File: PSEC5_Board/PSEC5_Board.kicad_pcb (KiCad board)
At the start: 2 copper layers, 76.2 x 76.2 mm, 187 parts, among them IC1 LTC6409IUDB#TRMPBF, IC2 LTC6409IUDB#TRMPBF, IC3 LTC6409IUDB#TRMPBF, IC4 LTC6409IUDB#TRMPBF, IC5 LTC6409IUDB#TRMPBF, IC6 LTC6409IUDB#TRMPBF, IC7 LTC6409IUDB#TRMPBF, IC8 LTC6409IUDB#TRMPBF, J1 QTH-040-01-X-D-DP-A, J11 Conn_Coaxial, J2 Conn_Coaxial, J3 Conn_Coaxial, J4 Conn_Coaxial, J5 Conn_Coaxial, J6 Conn_Coaxial, J7 Conn_Coaxial, J8 Conn_Coaxial, J9 QTH-040-01-X-D-DP-A, U1 MCP1700T-1802E_TT, U3 DAC8411IDCKT, U5 MC100LVEL, U6 OPA607QDBVRQ1, U7 AD4008BCPZ-RL7, Y1 ASE2-40.000MHZ-ET

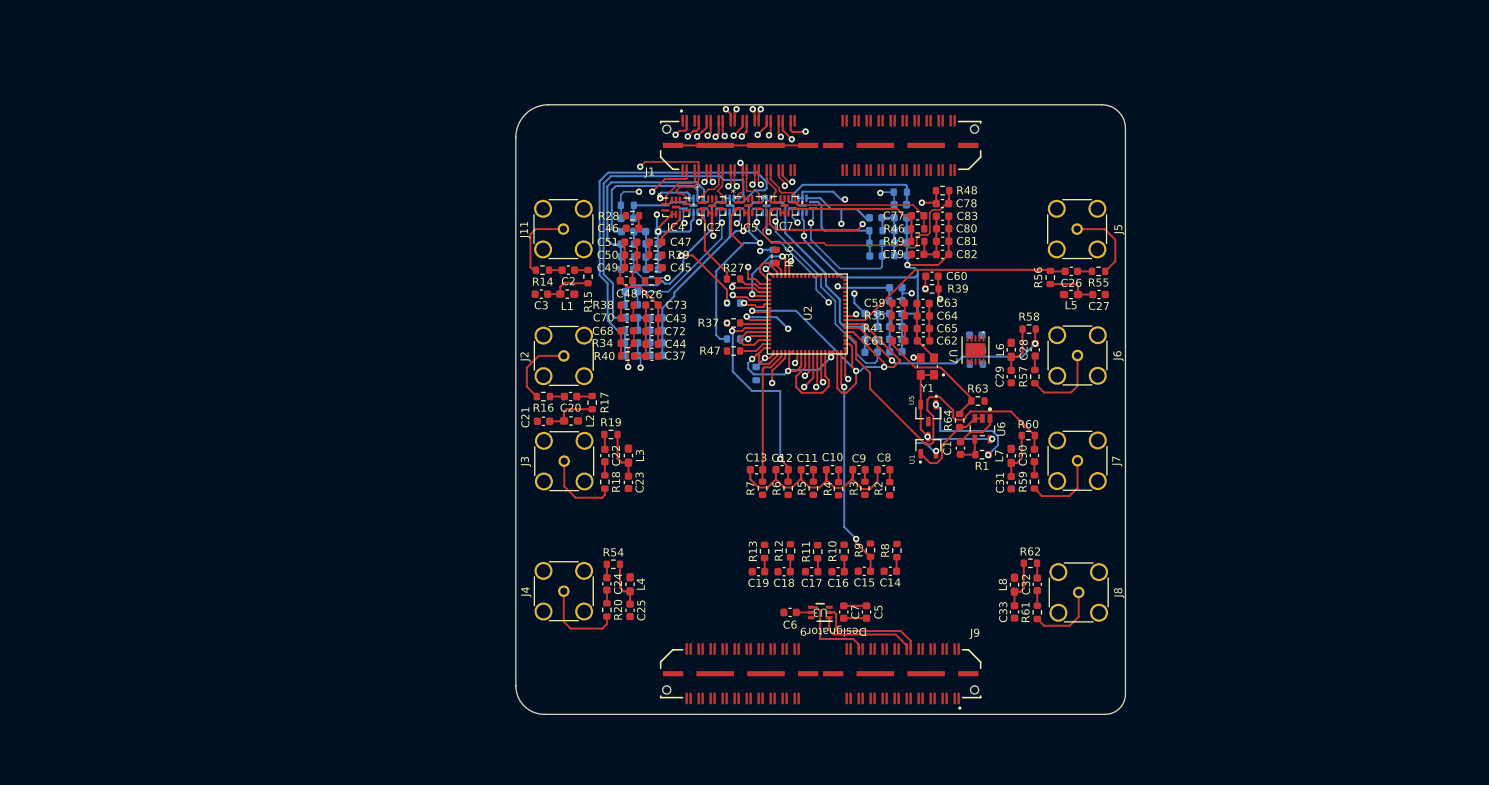
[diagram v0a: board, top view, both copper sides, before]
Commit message: DUT Layout Overhaul
Footprints need to be replaced.
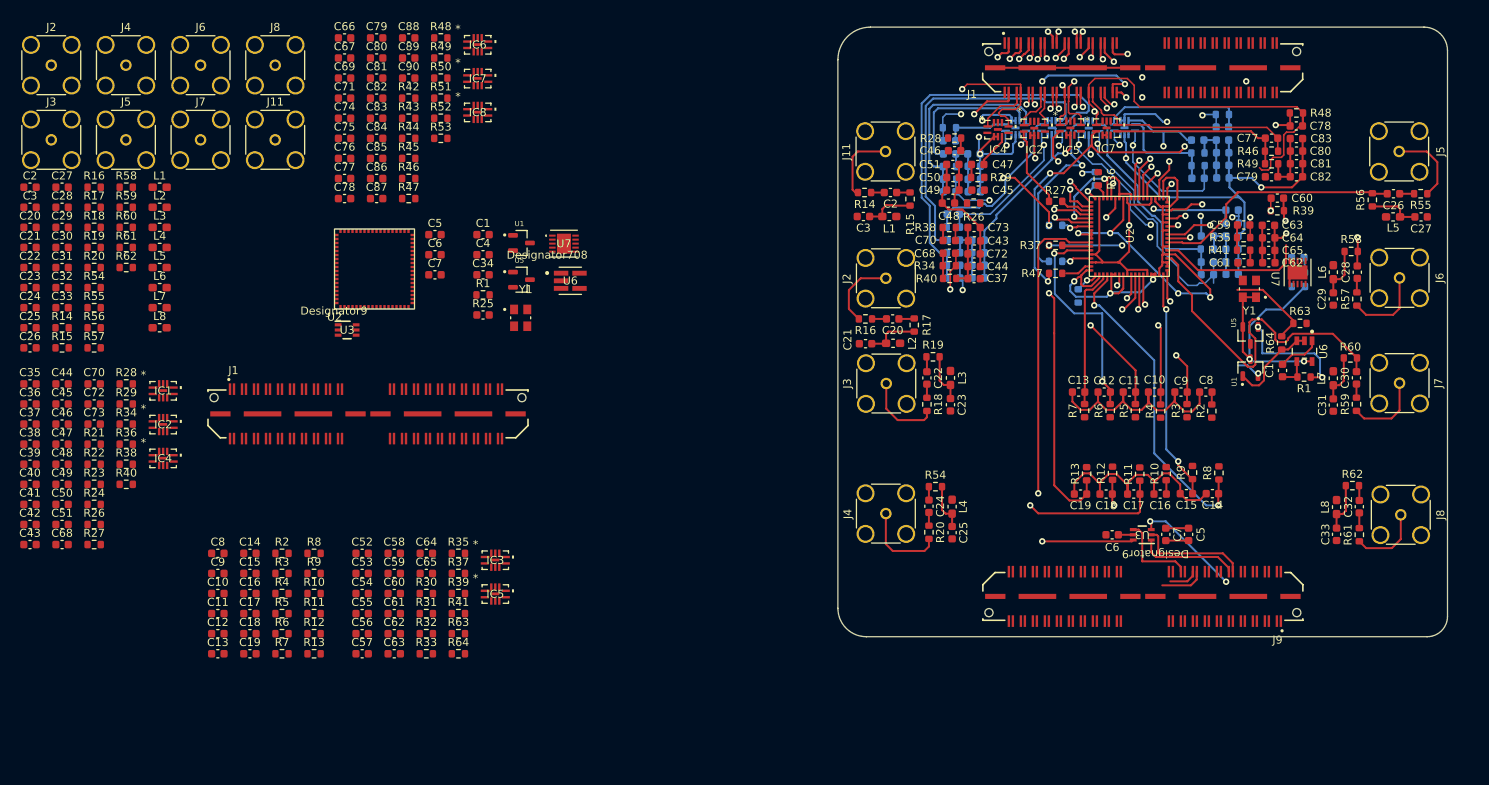
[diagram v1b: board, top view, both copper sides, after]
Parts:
- removed the C1 at (168.1, 81.5)
- removed the C10 at (152.1, 84.2)
- removed the C11 at (149.0, 84.2)
- removed the C12 at (145.8, 84.2)
- removed the C13 at (142.6, 84.2)
- removed the C14 at (159.4, 96.9)
- removed the C15 at (156.1, 96.9)
- removed the C16 at (152.8, 96.9)
- removed the C17 at (149.5, 96.9)
- removed the C18 at (146.1, 96.9)
- removed the C19 at (142.9, 96.9)
- removed the C2 at (119.1, 59.2)
- removed the C20 at (119.4, 75.0)
- removed the C21 at (116.0, 78.1)
- removed the C22 at (123.7, 82.4)
- removed the C23 at (126.6, 85.8)
- removed the C24 at (123.9, 98.4)
- removed the C25 at (126.8, 101.7)
- removed the C26 at (182.0, 59.4)
- removed the C27 at (185.4, 62.3)
- removed the C28 at (177.5, 69.2)
- removed the C29 at (174.5, 72.5)
- removed the C3 at (115.7, 62.2)
- removed the C30 at (177.4, 82.4)
- removed the C31 at (174.5, 85.8)
- removed the C32 at (177.7, 98.5)
- removed the C33 at (174.9, 101.9)
- removed the C34 at (170.0, 67.4)
- removed the C35 at (126.5, 59.1)
- removed the C36 at (126.5, 52.7)
- removed the C37 at (129.6, 70.0)
- removed the C38 at (126.5, 54.4)
- removed the C39 at (129.6, 55.9)
- removed the C4 at (170.1, 69.2)
- removed the C40 at (129.6, 57.6)
- removed the C41 at (129.6, 59.1)
- removed the C42 at (129.5, 54.4)
- removed the C43 at (129.6, 65.3)
- removed the C44 at (129.6, 68.5)
- removed the C45 at (130.1, 58.9)
- removed the C46 at (127.1, 54.0)
- removed the C47 at (130.0, 55.7)
- removed the C48 at (126.4, 60.5)
- removed the C49 at (126.9, 58.9)
- removed the C5 at (156.4, 102.0)
- removed the C50 at (126.9, 57.3)
- removed the C51 at (126.9, 55.7)
- removed the C52 at (127.0, 69.9)
- removed the C53 at (127.0, 61.9)
- removed the C54 at (127.0, 65.2)
- removed the C55 at (130.1, 65.2)
- removed the C56 at (130.1, 66.8)
- removed the C57 at (130.1, 68.3)
- removed the C58 at (130.1, 69.9)
- removed the C59 at (160.3, 63.3)
- removed the C6 at (146.8, 102.0)
- removed the C60 at (164.6, 60.0)
- removed the C61 at (160.4, 68.1)
- removed the C62 at (163.5, 68.1)
- removed the C63 at (163.4, 63.4)
- removed the C64 at (163.5, 64.9)
- removed the C65 at (163.5, 66.5)
- removed the C66 at (156.9, 69.5)
- removed the C67 at (160.0, 61.4)
- removed the C68 at (126.5, 66.8)
- removed the C69 at (157.0, 64.7)
- removed the C7 at (153.5, 102.0)
- removed the C70 at (126.5, 65.2)
- removed the C71 at (160.0, 69.4)
- removed the C72 at (129.6, 66.9)
- removed the C73 at (129.6, 63.6)
- removed the C74 at (160.0, 64.7)
- removed the C75 at (160.0, 67.9)
- removed the C76 at (160.0, 66.3)
- removed the C77 at (162.8, 52.4)
- removed the C78 at (165.9, 50.9)
- removed the C79 at (162.8, 57.3)
- removed the C8 at (158.5, 84.2)
- removed the C80 at (165.9, 54.0)
- removed the C81 at (165.9, 55.6)
- removed the C82 at (165.9, 57.3)
- removed the C83 at (165.9, 52.5)
- removed the C84 at (157.6, 57.4)
- removed the C85 at (160.6, 51.0)
- removed the C86 at (157.5, 52.7)
- removed the C87 at (160.6, 55.8)
- removed the C88 at (160.6, 54.2)
- removed the C89 at (160.6, 52.7)
- removed the C9 at (155.4, 84.2)
- removed the C90 at (160.7, 57.4)
- removed the IC1 at (134.8, 51.1)
- removed the IC2 at (137.1, 51.2)
- removed the IC3 at (139.3, 51.1)
- removed the IC4 at (132.5, 51.4)
- removed the IC5 at (141.6, 51.2)
- removed the IC6 at (143.9, 51.1)
- removed the IC7 at (146.1, 51.2)
- removed the IC8 at (148.4, 51.1)
- removed the J1 at (150.6, 43.6)
- removed the J11 at (118.5, 54.1)
- removed the J2 at (118.5, 69.9)
- removed the J3 at (118.6, 83.1)
- removed the J4 at (118.5, 99.4)
- removed the J5 at (182.7, 54.1)
- removed the J6 at (182.7, 69.9)
- removed the J7 at (182.7, 83.0)
- removed the J8 at (182.9, 99.5)
- removed the L1 at (119.0, 62.2)
- removed the L2 at (119.4, 78.1)
- removed the L3 at (126.6, 82.4)
- removed the L4 at (126.8, 98.5)
- removed the L5 at (181.9, 62.3)
- removed the L6 at (174.5, 69.2)
- removed the L7 at (174.5, 82.4)
- removed the L8 at (174.9, 98.5)
- removed the R1 at (170.8, 82.3)
- removed the R10 at (153.6, 94.4)
- removed the R11 at (150.3, 94.4)
- removed the R12 at (146.9, 94.3)
- removed the R13 at (143.6, 94.4)
- removed the R14 at (115.9, 59.2)
- removed the R15 at (121.6, 60.0)
- removed the R16 at (116.0, 75.0)
- removed the R17 at (122.1, 75.8)
- removed the R18 at (123.7, 85.7)
- removed the R19 at (124.4, 79.8)
- removed the R2 at (159.3, 86.5)
- removed the R20 at (123.9, 101.7)
- removed the R21 at (126.5, 57.5)
- removed the R22 at (144.7, 57.5)
- removed the R23 at (126.5, 51.1)
- removed the R24 at (126.5, 56.0)
- removed the R25 at (170.1, 71.0)
- removed the R26 at (129.5, 60.5)
- removed the R27 at (139.8, 60.3)
- removed the R28 at (127.1, 52.4)
- removed the R29 at (130.0, 57.3)
- removed the R3 at (156.2, 86.5)
- removed the R30 at (127.0, 68.3)
- removed the R31 at (139.8, 63.3)
- removed the R32 at (127.0, 63.5)
- removed the R33 at (127.0, 66.7)
- removed the R34 at (126.5, 68.4)
- removed the R35 at (160.3, 64.9)
- removed the R36 at (145.1, 57.5)
- removed the R37 at (139.8, 65.8)
- removed the R38 at (126.5, 63.6)
- removed the R39 at (164.6, 61.6)
- removed the R4 at (152.9, 86.5)
- removed the R40 at (126.5, 70.0)
- removed the R41 at (160.3, 66.5)
- removed the R42 at (156.9, 67.9)
- removed the R43 at (139.8, 67.8)
- removed the R44 at (160.0, 63.0)
- removed the R45 at (156.9, 66.3)
- removed the R46 at (162.8, 54.1)
- removed the R47 at (139.8, 69.3)
- removed the R48 at (165.9, 49.3)
- removed the R49 at (162.8, 55.6)
- removed the R5 at (149.7, 86.5)
- removed the R50 at (157.6, 55.9)
- removed the R51 at (142.6, 72.1)
- removed the R52 at (160.6, 49.5)
- removed the R53 at (157.5, 54.3)
- removed the R54 at (124.7, 96.0)
- removed the R55 at (185.4, 59.4)
- removed the R56 at (179.3, 60.1)
- removed the R57 at (177.4, 72.5)
- removed the R58 at (176.7, 66.6)
- removed the R59 at (177.4, 85.7)
- removed the R6 at (146.6, 86.5)
- removed the R60 at (176.6, 79.9)
- removed the R61 at (177.7, 102.0)
- removed the R62 at (176.9, 95.9)
- removed the R63 at (170.3, 75.6)
- removed the R64 at (168.0, 78.0)
- removed the R7 at (143.4, 86.5)
- removed the R8 at (160.2, 94.3)
- removed the R9 at (156.9, 94.2)
- removed the U1 at (164.1, 81.1)
- removed the U2 at (154.0, 59.7)
- removed the U3 at (150.6, 102.0)
- removed the U5 at (164.1, 77.1)
- removed the U6 at (170.9, 79.1)
- removed the U7 at (170.0, 69.2)
- removed the Y1 at (164.0, 71.3)
- added C1: C, Capacitor_SMD:C_0603_1608Metric, F.Cu at (108.4, 54.8)
- added C1: C, Capacitor_SMD:C_0603_1608Metric, F.Cu at (208.4, 71.8)
- added C10: C, Capacitor_SMD:C_0603_1608Metric, F.Cu at (192.4, 74.5)
- added C10: C, Capacitor_SMD:C_0603_1608Metric, F.Cu at (75.3, 99.6)
- added C11: C, Capacitor_SMD:C_0603_1608Metric, F.Cu at (75.3, 102.2)
- added C11: C, Capacitor_SMD:C_0603_1608Metric, F.Cu at (189.2, 74.5)
- added C12: C, Capacitor_SMD:C_0603_1608Metric, F.Cu at (75.3, 104.7)
- added C12: C, Capacitor_SMD:C_0603_1608Metric, F.Cu at (186.1, 74.5)
- added C13: C, Capacitor_SMD:C_0603_1608Metric, F.Cu at (75.3, 107.2)
- added C13: C, Capacitor_SMD:C_0603_1608Metric, F.Cu at (182.9, 74.5)
- added C14: C, Capacitor_SMD:C_0603_1608Metric, F.Cu at (79.3, 94.6)
- added C14: C, Capacitor_SMD:C_0603_1608Metric, F.Cu at (199.6, 87.2)
- added C15: C, Capacitor_SMD:C_0603_1608Metric, F.Cu at (79.3, 97.1)
- added C15: C, Capacitor_SMD:C_0603_1608Metric, F.Cu at (196.4, 87.2)
- added C16: C, Capacitor_SMD:C_0603_1608Metric, F.Cu at (193.1, 87.2)
- added C16: C, Capacitor_SMD:C_0603_1608Metric, F.Cu at (79.3, 99.6)
- added C17: C, Capacitor_SMD:C_0603_1608Metric, F.Cu at (79.3, 102.2)
- added C17: C, Capacitor_SMD:C_0603_1608Metric, F.Cu at (189.8, 87.2)
- added C18: C, Capacitor_SMD:C_0603_1608Metric, F.Cu at (186.3, 87.2)
- added C18: C, Capacitor_SMD:C_0603_1608Metric, F.Cu at (79.3, 104.7)
- added C19: C, Capacitor_SMD:C_0603_1608Metric, F.Cu at (183.1, 87.2)
- added C19: C, Capacitor_SMD:C_0603_1608Metric, F.Cu at (79.3, 107.2)
- added C2: 100n, Capacitor_SMD:C_0603_1608Metric, F.Cu at (51.8, 48.9)
- added C2: 100n, Capacitor_SMD:C_0603_1608Metric, F.Cu at (159.4, 49.5)
- added C20: 100n, Capacitor_SMD:C_0603_1608Metric, F.Cu at (51.8, 53.9)
- added C20: 100n, Capacitor_SMD:C_0603_1608Metric, F.Cu at (159.6, 65.3)
- added C21: 100n, Capacitor_SMD:C_0603_1608Metric, F.Cu at (51.8, 56.4)
- added C21: 100n, Capacitor_SMD:C_0603_1608Metric, F.Cu at (156.3, 68.4)
- added C22: 100n, Capacitor_SMD:C_0603_1608Metric, F.Cu at (163.9, 72.7)
- added C22: 100n, Capacitor_SMD:C_0603_1608Metric, F.Cu at (51.8, 58.9)
- added C23: 100n, Capacitor_SMD:C_0603_1608Metric, F.Cu at (51.8, 61.4)
- added C23: 100n, Capacitor_SMD:C_0603_1608Metric, F.Cu at (166.9, 76.0)
- added C24: 100n, Capacitor_SMD:C_0603_1608Metric, F.Cu at (164.2, 88.7)
- added C24: 100n, Capacitor_SMD:C_0603_1608Metric, F.Cu at (51.8, 63.9)
- added C25: 100n, Capacitor_SMD:C_0603_1608Metric, F.Cu at (51.8, 66.4)
- added C25: 100n, Capacitor_SMD:C_0603_1608Metric, F.Cu at (167.1, 92.0)
- added C26: 100n, Capacitor_SMD:C_0603_1608Metric, F.Cu at (51.8, 68.9)
- added C26: 100n, Capacitor_SMD:C_0603_1608Metric, F.Cu at (222.2, 49.7)
- added C27: 100n, Capacitor_SMD:C_0603_1608Metric, F.Cu at (55.8, 48.9)
- added C27: 100n, Capacitor_SMD:C_0603_1608Metric, F.Cu at (225.7, 52.6)
- added C28: 100n, Capacitor_SMD:C_0603_1608Metric, F.Cu at (217.7, 59.5)
- added C28: 100n, Capacitor_SMD:C_0603_1608Metric, F.Cu at (55.8, 51.4)
- added C29: 100n, Capacitor_SMD:C_0603_1608Metric, F.Cu at (55.8, 53.9)
- added C29: 100n, Capacitor_SMD:C_0603_1608Metric, F.Cu at (214.7, 62.8)
- added C3: 100n, Capacitor_SMD:C_0603_1608Metric, F.Cu at (51.8, 51.4)
- added C3: 100n, Capacitor_SMD:C_0603_1608Metric, F.Cu at (156.0, 52.5)
- added C30: 100n, Capacitor_SMD:C_0603_1608Metric, F.Cu at (55.8, 56.4)
- added C30: 100n, Capacitor_SMD:C_0603_1608Metric, F.Cu at (217.6, 72.7)
- added C31: 100n, Capacitor_SMD:C_0603_1608Metric, F.Cu at (214.7, 76.1)
- added C31: 100n, Capacitor_SMD:C_0603_1608Metric, F.Cu at (55.8, 58.9)
- added C32: 100n, Capacitor_SMD:C_0603_1608Metric, F.Cu at (55.8, 61.4)
- added C32: 100n, Capacitor_SMD:C_0603_1608Metric, F.Cu at (218.0, 88.8)
- added C33: 100n, Capacitor_SMD:C_0603_1608Metric, F.Cu at (215.1, 92.2)
- added C33: 100n, Capacitor_SMD:C_0603_1608Metric, F.Cu at (55.8, 63.9)
- added C34: C, Capacitor_SMD:C_0603_1608Metric, F.Cu at (108.4, 59.8)
- added C34: C, Capacitor_SMD:C_0603_1608Metric, B.Cu at (210.3, 57.7)
- added C35: 1.3pF, Capacitor_SMD:C_0603_1608Metric, F.Cu at (51.8, 73.4)
- added C35: 1.3pF, Capacitor_SMD:C_0603_1608Metric, B.Cu at (166.8, 49.4)
- added C36: 1.3pF, Capacitor_SMD:C_0603_1608Metric, F.Cu at (51.8, 76.0)
- added C36: 1.3pF, Capacitor_SMD:C_0603_1608Metric, B.Cu at (166.7, 43.0)
- added C37: 0.1u, Capacitor_SMD:C_0603_1608Metric, F.Cu at (169.8, 60.3)
- added C37: 0.1u, Capacitor_SMD:C_0603_1608Metric, F.Cu at (51.8, 78.5)
- added C38: 0.1u, Capacitor_SMD:C_0603_1608Metric, F.Cu at (51.8, 81.0)
- added C38: 0.1u, Capacitor_SMD:C_0603_1608Metric, B.Cu at (166.8, 44.7)
- added C39: 1000pF, Capacitor_SMD:C_0603_1608Metric, F.Cu at (51.8, 83.5)
- added C39: 1000pF, Capacitor_SMD:C_0603_1608Metric, B.Cu at (169.8, 46.2)
- added C4: 0.1 uf, Capacitor_SMD:C_0603_1608Metric, F.Cu at (108.4, 57.3)
- added C4: 0.1 uf, Capacitor_SMD:C_0603_1608Metric, B.Cu at (210.4, 59.5)
- added C40: 0.1uF, Capacitor_SMD:C_0603_1608Metric, F.Cu at (51.8, 86.0)
- added C40: 0.1uF, Capacitor_SMD:C_0603_1608Metric, B.Cu at (169.8, 47.9)
- added C41: 0.1uF, Capacitor_SMD:C_0603_1608Metric, F.Cu at (51.8, 88.5)
- added C41: 0.1uF, Capacitor_SMD:C_0603_1608Metric, B.Cu at (169.9, 49.4)
- added C42: 1000pF, Capacitor_SMD:C_0603_1608Metric, F.Cu at (51.8, 91.0)
- added C42: 1000pF, Capacitor_SMD:C_0603_1608Metric, B.Cu at (169.8, 44.7)
- added C43: 0.1uF, Capacitor_SMD:C_0603_1608Metric, F.Cu at (169.9, 55.6)
- added C43: 0.1uF, Capacitor_SMD:C_0603_1608Metric, F.Cu at (51.8, 93.5)
- added C44: 1000pF, Capacitor_SMD:C_0603_1608Metric, F.Cu at (169.8, 58.8)
- added C44: 1000pF, Capacitor_SMD:C_0603_1608Metric, F.Cu at (55.8, 73.4)
- added C45: 1.3pF, Capacitor_SMD:C_0603_1608Metric, F.Cu at (55.8, 76.0)
- added C45: 1.3pF, Capacitor_SMD:C_0603_1608Metric, F.Cu at (170.3, 49.2)
- added C46: 1.3pF, Capacitor_SMD:C_0603_1608Metric, F.Cu at (167.4, 44.3)
- added C46: 1.3pF, Capacitor_SMD:C_0603_1608Metric, F.Cu at (55.8, 78.5)
- added C47: 0.1u, Capacitor_SMD:C_0603_1608Metric, F.Cu at (170.3, 46.0)
- added C47: 0.1u, Capacitor_SMD:C_0603_1608Metric, F.Cu at (55.8, 81.0)
- added C48: 1000pF, Capacitor_SMD:C_0603_1608Metric, F.Cu at (55.8, 83.5)
- added C48: 1000pF, Capacitor_SMD:C_0603_1608Metric, F.Cu at (166.6, 50.8)
- added C49: 0.1uF, Capacitor_SMD:C_0603_1608Metric, F.Cu at (167.2, 49.2)
- added C49: 0.1uF, Capacitor_SMD:C_0603_1608Metric, F.Cu at (55.8, 86.0)
- added C5: 700n, Capacitor_SMD:C_0603_1608Metric, F.Cu at (196.6, 92.2)
- added C5: 700n, Capacitor_SMD:C_0603_1608Metric, F.Cu at (102.4, 54.8)
- added C50: 0.1uF, Capacitor_SMD:C_0603_1608Metric, F.Cu at (55.8, 88.5)
- added C50: 0.1uF, Capacitor_SMD:C_0603_1608Metric, F.Cu at (167.2, 47.6)
- added C51: 1000pF, Capacitor_SMD:C_0603_1608Metric, F.Cu at (167.2, 46.0)
- added C51: 1000pF, Capacitor_SMD:C_0603_1608Metric, F.Cu at (55.8, 91.0)
- added C52: 1.3pF, Capacitor_SMD:C_0603_1608Metric, F.Cu at (93.3, 94.6)
- added C52: 1.3pF, Capacitor_SMD:C_0603_1608Metric, B.Cu at (167.3, 60.2)
- added C53: 1.3pF, Capacitor_SMD:C_0603_1608Metric, F.Cu at (93.3, 97.1)
- added C53: 1.3pF, Capacitor_SMD:C_0603_1608Metric, B.Cu at (167.2, 52.2)
- added C54: 0.1u, Capacitor_SMD:C_0603_1608Metric, F.Cu at (93.3, 99.6)
- added C54: 0.1u, Capacitor_SMD:C_0603_1608Metric, B.Cu at (167.3, 55.5)
- added C55: 1000pF, Capacitor_SMD:C_0603_1608Metric, F.Cu at (93.3, 102.2)
- added C55: 1000pF, Capacitor_SMD:C_0603_1608Metric, B.Cu at (170.3, 55.5)
- added C56: 0.1uF, Capacitor_SMD:C_0603_1608Metric, F.Cu at (93.3, 104.7)
- added C56: 0.1uF, Capacitor_SMD:C_0603_1608Metric, B.Cu at (170.3, 57.1)
- added C57: 0.1uF, Capacitor_SMD:C_0603_1608Metric, F.Cu at (93.3, 107.2)
- added C57: 0.1uF, Capacitor_SMD:C_0603_1608Metric, B.Cu at (170.4, 58.6)
- added C58: 1000pF, Capacitor_SMD:C_0603_1608Metric, F.Cu at (97.3, 94.6)
- added C58: 1000pF, Capacitor_SMD:C_0603_1608Metric, B.Cu at (170.4, 60.2)
- added C59: 1.3pF, Capacitor_SMD:C_0603_1608Metric, F.Cu at (203.5, 53.6)
- added C59: 1.3pF, Capacitor_SMD:C_0603_1608Metric, F.Cu at (97.3, 97.1)
- added C6: 400n, Capacitor_SMD:C_0603_1608Metric, F.Cu at (102.4, 57.3)
- added C6: 400n, Capacitor_SMD:C_0603_1608Metric, F.Cu at (187.1, 92.3)
- added C60: 1.3pF, Capacitor_SMD:C_0603_1608Metric, F.Cu at (97.3, 99.6)
- added C60: 1.3pF, Capacitor_SMD:C_0603_1608Metric, F.Cu at (207.7, 50.2)
- added C61: 0.1u, Capacitor_SMD:C_0603_1608Metric, F.Cu at (203.6, 58.3)
- added C61: 0.1u, Capacitor_SMD:C_0603_1608Metric, F.Cu at (97.3, 102.2)
- added C62: 1000pF, Capacitor_SMD:C_0603_1608Metric, F.Cu at (206.7, 58.3)
- added C62: 1000pF, Capacitor_SMD:C_0603_1608Metric, F.Cu at (97.3, 104.7)
- added C63: 0.1uF, Capacitor_SMD:C_0603_1608Metric, F.Cu at (97.3, 107.2)
- added C63: 0.1uF, Capacitor_SMD:C_0603_1608Metric, F.Cu at (206.6, 53.6)
- added C64: 0.1uF, Capacitor_SMD:C_0603_1608Metric, F.Cu at (101.4, 94.6)
- added C64: 0.1uF, Capacitor_SMD:C_0603_1608Metric, F.Cu at (206.6, 55.2)
- added C65: 1000pF, Capacitor_SMD:C_0603_1608Metric, F.Cu at (206.6, 56.8)
- added C65: 1000pF, Capacitor_SMD:C_0603_1608Metric, F.Cu at (101.4, 97.1)
- added C66: 1.3pF, Capacitor_SMD:C_0603_1608Metric, F.Cu at (91.1, 30.2)
- added C66: 1.3pF, Capacitor_SMD:C_0603_1608Metric, B.Cu at (199.0, 59.8)
- added C67: 1.3pF, Capacitor_SMD:C_0603_1608Metric, F.Cu at (91.1, 32.7)
- added C67: 1.3pF, Capacitor_SMD:C_0603_1608Metric, B.Cu at (202.1, 51.7)
- added C68: 1.3pF, Capacitor_SMD:C_0603_1608Metric, F.Cu at (166.7, 57.1)
- added C68: 1.3pF, Capacitor_SMD:C_0603_1608Metric, F.Cu at (55.8, 93.5)
- added C69: 0.1u, Capacitor_SMD:C_0603_1608Metric, F.Cu at (91.1, 35.2)
- added C69: 0.1u, Capacitor_SMD:C_0603_1608Metric, B.Cu at (199.0, 55.0)
- added C7: 100n, Capacitor_SMD:C_0603_1608Metric, F.Cu at (102.4, 59.8)
- added C7: 100n, Capacitor_SMD:C_0603_1608Metric, F.Cu at (193.8, 92.2)
- added C70: 1.3pF, Capacitor_SMD:C_0603_1608Metric, F.Cu at (59.8, 73.4)
- added C70: 1.3pF, Capacitor_SMD:C_0603_1608Metric, F.Cu at (166.7, 55.5)
- added C71: 1000pF, Capacitor_SMD:C_0603_1608Metric, F.Cu at (91.1, 37.7)
- added C71: 1000pF, Capacitor_SMD:C_0603_1608Metric, B.Cu at (202.1, 59.7)
- added C72: 1000pF, Capacitor_SMD:C_0603_1608Metric, F.Cu at (169.8, 57.2)
- added C72: 1000pF, Capacitor_SMD:C_0603_1608Metric, F.Cu at (59.8, 76.0)
- added C73: 0.1uF, Capacitor_SMD:C_0603_1608Metric, F.Cu at (59.8, 78.5)
- added C73: 0.1uF, Capacitor_SMD:C_0603_1608Metric, F.Cu at (169.8, 53.9)
- added C74: 0.1uF, Capacitor_SMD:C_0603_1608Metric, F.Cu at (91.1, 40.2)
- added C74: 0.1uF, Capacitor_SMD:C_0603_1608Metric, B.Cu at (202.1, 55.0)
- added C75: 0.1uF, Capacitor_SMD:C_0603_1608Metric, F.Cu at (91.1, 42.7)
- added C75: 0.1uF, Capacitor_SMD:C_0603_1608Metric, B.Cu at (202.1, 58.2)
- added C76: 1000pF, Capacitor_SMD:C_0603_1608Metric, F.Cu at (91.1, 45.2)
- added C76: 1000pF, Capacitor_SMD:C_0603_1608Metric, B.Cu at (202.1, 56.6)
- added C77: 1.3pF, Capacitor_SMD:C_0603_1608Metric, F.Cu at (91.1, 47.8)
- added C77: 1.3pF, Capacitor_SMD:C_0603_1608Metric, F.Cu at (207.0, 42.7)
- added C78: 1.3pF, Capacitor_SMD:C_0603_1608Metric, F.Cu at (91.1, 50.3)
- added C78: 1.3pF, Capacitor_SMD:C_0603_1608Metric, F.Cu at (210.1, 41.2)
- added C79: 0.1u, Capacitor_SMD:C_0603_1608Metric, F.Cu at (95.1, 30.2)
- added C79: 0.1u, Capacitor_SMD:C_0603_1608Metric, F.Cu at (207.0, 47.5)
- added C8: C, Capacitor_SMD:C_0603_1608Metric, F.Cu at (75.3, 94.6)
- added C8: C, Capacitor_SMD:C_0603_1608Metric, F.Cu at (198.8, 74.5)
- added C80: 1000pF, Capacitor_SMD:C_0603_1608Metric, F.Cu at (95.1, 32.7)
- added C80: 1000pF, Capacitor_SMD:C_0603_1608Metric, F.Cu at (210.1, 44.3)
- added C81: 0.1uF, Capacitor_SMD:C_0603_1608Metric, F.Cu at (210.1, 45.9)
- added C81: 0.1uF, Capacitor_SMD:C_0603_1608Metric, F.Cu at (95.1, 35.2)
- added C82: 0.1uF, Capacitor_SMD:C_0603_1608Metric, F.Cu at (210.1, 47.5)
- added C82: 0.1uF, Capacitor_SMD:C_0603_1608Metric, F.Cu at (95.1, 37.7)
- added C83: 1000pF, Capacitor_SMD:C_0603_1608Metric, F.Cu at (210.1, 42.8)
- added C83: 1000pF, Capacitor_SMD:C_0603_1608Metric, F.Cu at (95.1, 40.2)
- added C84: 1.3pF, Capacitor_SMD:C_0603_1608Metric, F.Cu at (95.1, 42.7)
- added C84: 1.3pF, Capacitor_SMD:C_0603_1608Metric, B.Cu at (197.8, 47.7)
- added C85: 1.3pF, Capacitor_SMD:C_0603_1608Metric, F.Cu at (95.1, 45.2)
- added C85: 1.3pF, Capacitor_SMD:C_0603_1608Metric, B.Cu at (200.9, 41.3)
- added C86: 0.1u, Capacitor_SMD:C_0603_1608Metric, F.Cu at (95.1, 47.8)
- added C86: 0.1u, Capacitor_SMD:C_0603_1608Metric, B.Cu at (197.8, 43.0)
- added C87: 1000pF, Capacitor_SMD:C_0603_1608Metric, F.Cu at (95.1, 50.3)
- added C87: 1000pF, Capacitor_SMD:C_0603_1608Metric, B.Cu at (200.9, 46.1)
- added C88: 0.1uF, Capacitor_SMD:C_0603_1608Metric, F.Cu at (99.2, 30.2)
- added C88: 0.1uF, Capacitor_SMD:C_0603_1608Metric, B.Cu at (200.9, 44.5)
- added C89: 0.1uF, Capacitor_SMD:C_0603_1608Metric, F.Cu at (99.2, 32.7)
- added C89: 0.1uF, Capacitor_SMD:C_0603_1608Metric, B.Cu at (200.9, 43.0)
- added C9: C, Capacitor_SMD:C_0603_1608Metric, F.Cu at (75.3, 97.1)
- added C9: C, Capacitor_SMD:C_0603_1608Metric, F.Cu at (195.7, 74.5)
- added C90: 1000pF, Capacitor_SMD:C_0603_1608Metric, F.Cu at (99.2, 35.2)
- added C90: 1000pF, Capacitor_SMD:C_0603_1608Metric, B.Cu at (200.9, 47.7)
- added IC1: LTC6409IUDB#TRMPBF, LTC6409IUDB_TRMPBF:QFN-10_UDB_LIT, F.Cu at (68.5, 74.3)
- added IC1: LTC6409IUDB#TRMPBF, LTC6409IUDB#TRMPBF:QFN-10_UDB_LIT, B.Cu at (175.0, 41.4)
- added IC2: LTC6409IUDB#TRMPBF, LTC6409IUDB_TRMPBF:QFN-10_UDB_LIT, F.Cu at (68.5, 78.5)
- added IC2: LTC6409IUDB#TRMPBF, LTC6409IUDB#TRMPBF:QFN-10_UDB_LIT, F.Cu at (177.3, 41.5)
- added IC3: LTC6409IUDB#TRMPBF, LTC6409IUDB_TRMPBF:QFN-10_UDB_LIT, F.Cu at (110.0, 95.5)
- added IC3: LTC6409IUDB#TRMPBF, LTC6409IUDB#TRMPBF:QFN-10_UDB_LIT, B.Cu at (179.5, 41.4)
- added IC4: LTC6409IUDB#TRMPBF, LTC6409IUDB_TRMPBF:QFN-10_UDB_LIT, F.Cu at (68.5, 82.7)
- added IC4: LTC6409IUDB#TRMPBF, LTC6409IUDB#TRMPBF:QFN-10_UDB_LIT, F.Cu at (172.8, 41.7)
- added IC5: LTC6409IUDB#TRMPBF, LTC6409IUDB#TRMPBF:QFN-10_UDB_LIT, F.Cu at (181.9, 41.5)
- added IC5: LTC6409IUDB#TRMPBF, LTC6409IUDB_TRMPBF:QFN-10_UDB_LIT, F.Cu at (110.0, 99.7)
- added IC6: LTC6409IUDB#TRMPBF, LTC6409IUDB_TRMPBF:QFN-10_UDB_LIT, F.Cu at (107.8, 31.0)
- added IC6: LTC6409IUDB#TRMPBF, LTC6409IUDB#TRMPBF:QFN-10_UDB_LIT, B.Cu at (184.2, 41.4)
- added IC7: LTC6409IUDB#TRMPBF, LTC6409IUDB#TRMPBF:QFN-10_UDB_LIT, F.Cu at (186.4, 41.5)
- added IC7: LTC6409IUDB#TRMPBF, LTC6409IUDB_TRMPBF:QFN-10_UDB_LIT, F.Cu at (107.8, 35.3)
- added IC8: LTC6409IUDB#TRMPBF, LTC6409IUDB_TRMPBF:QFN-10_UDB_LIT, F.Cu at (107.8, 39.5)
- added IC8: LTC6409IUDB#TRMPBF, LTC6409IUDB#TRMPBF:QFN-10_UDB_LIT, B.Cu at (188.6, 41.4)
- added J1: QTH-040-01-X-D-DP-A, QTH-040-01-X-D-DP-A:SAMTEC_QTH-040-01-X-D-DP-A, F.Cu at (94.1, 77.2)
- added J1: QTH-040-01-X-D-DP-A, QTH-040-01-X-D-DP-A:SAMTEC_QTH-040-01-X-D-DP-A, F.Cu at (190.9, 33.9)
- added J11: Conn_Coaxial, Connector_Coaxial:SMA_Amphenol_132134-14_Vertical, F.Cu at (82.5, 42.9)
- added J11: Conn_Coaxial, Connector_Coaxial:SMA_Amphenol_132134-14_Vertical, F.Cu at (158.7, 44.4)
- added J2: Conn_Coaxial, Connector_Coaxial:SMA_Amphenol_132134-14_Vertical, F.Cu at (54.5, 33.6)
- added J2: Conn_Coaxial, Connector_Coaxial:SMA_Amphenol_132134-14_Vertical, F.Cu at (158.8, 60.2)
- added J3: Conn_Coaxial, Connector_Coaxial:SMA_Amphenol_132134-14_Vertical, F.Cu at (158.8, 73.4)
- added J3: Conn_Coaxial, Connector_Coaxial:SMA_Amphenol_132134-14_Vertical, F.Cu at (54.5, 42.9)
- added J4: Conn_Coaxial, Connector_Coaxial:SMA_Amphenol_132134-14_Vertical, F.Cu at (158.8, 89.6)
- added J4: Conn_Coaxial, Connector_Coaxial:SMA_Amphenol_132134-14_Vertical, F.Cu at (63.8, 33.6)
- added J5: Conn_Coaxial, Connector_Coaxial:SMA_Amphenol_132134-14_Vertical, F.Cu at (63.8, 42.9)
- added J5: Conn_Coaxial, Connector_Coaxial:SMA_Amphenol_132134-14_Vertical, F.Cu at (223.0, 44.4)
- added J6: Conn_Coaxial, Connector_Coaxial:SMA_Amphenol_132134-14_Vertical, F.Cu at (223.0, 60.2)
- added J6: Conn_Coaxial, Connector_Coaxial:SMA_Amphenol_132134-14_Vertical, F.Cu at (73.1, 33.6)
- added J7: Conn_Coaxial, Connector_Coaxial:SMA_Amphenol_132134-14_Vertical, F.Cu at (223.0, 73.3)
- added J7: Conn_Coaxial, Connector_Coaxial:SMA_Amphenol_132134-14_Vertical, F.Cu at (73.1, 42.9)
- added J8: Conn_Coaxial, Connector_Coaxial:SMA_Amphenol_132134-14_Vertical, F.Cu at (82.5, 33.6)
- added J8: Conn_Coaxial, Connector_Coaxial:SMA_Amphenol_132134-14_Vertical, F.Cu at (223.2, 89.8)
- added L1: 10u, Inductor_SMD:L_0603_1608Metric_Pad1.05x0.95mm_HandSolder, F.Cu at (68.0, 48.9)
- added L1: 10u, Inductor_SMD:L_0603_1608Metric_Pad1.05x0.95mm_HandSolder, F.Cu at (159.2, 52.5)
- added L2: 10u, Inductor_SMD:L_0603_1608Metric_Pad1.05x0.95mm_HandSolder, F.Cu at (68.0, 51.4)
- added L2: 10u, Inductor_SMD:L_0603_1608Metric_Pad1.05x0.95mm_HandSolder, F.Cu at (159.7, 68.4)
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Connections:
- J9 pad 01: (no net) -> unconnected-(J9-Pad01)
- J9 pad 02: (no net) -> V_ped1
- J9 pad 03: (no net) -> unconnected-(J9-Pad03)
- J9 pad 04: (no net) -> V_ped2
- J9 pad 05: (no net) -> unconnected-(J9-Pad05)
- J9 pad 06: (no net) -> V_ped3
- J9 pad 07: (no net) -> unconnected-(J9-Pad07)
- J9 pad 08: (no net) -> V_ped4
- J9 pad 09: (no net) -> unconnected-(J9-Pad09)
- J9 pad 10: (no net) -> V_ped5
- J9 pad 11: (no net) -> unconnected-(J9-Pad11)
- J9 pad 12: (no net) -> V_ped6
- J9 pad 13: (no net) -> unconnected-(J9-Pad13)
- J9 pad 14: (no net) -> V_ped7
- J9 pad 15: (no net) -> unconnected-(J9-Pad15)
- J9 pad 16: (no net) -> V_ped8
- J9 pad 17: (no net) -> unconnected-(J9-Pad17)
- J9 pad 18: (no net) -> DAC_SCLK
- J9 pad 19: (no net) -> unconnected-(J9-Pad19)
- J9 pad 20: (no net) -> SYNC_N
- J9 pad 21: (no net) -> unconnected-(J9-Pad21)
- J9 pad 22: (no net) -> DAC_V_IN
- J9 pad 23: (no net) -> unconnected-(J9-Pad23)
- J9 pad 24: (no net) -> ADC_SCK
- J9 pad 25: (no net) -> unconnected-(J9-Pad25)
- J9 pad 26: (no net) -> ADC_SDO
- J9 pad 27: (no net) -> unconnected-(J9-Pad27)
- J9 pad 28: (no net) -> ADC_CNV
- J9 pad 29: (no net) -> unconnected-(J9-Pad29)
- J9 pad 30: (no net) -> VDD
- J9 pad 31: (no net) -> unconnected-(J9-Pad31)
- J9 pad 32: (no net) -> VDD18
- J9 pad 33: (no net) -> unconnected-(J9-Pad33)
- J9 pad 34: (no net) -> VDD33
- J9 pad 35: (no net) -> unconnected-(J9-Pad35)
- J9 pad 36: (no net) -> VDD25
- J9 pad 37: (no net) -> unconnected-(J9-Pad37)
- J9 pad 38: (no net) -> VDD50
- J9 pad 39: (no net) -> unconnected-(J9-Pad39)
- J9 pad 40: (no net) -> unconnected-(J9-Pad40)
- J9 pad 41: (no net) -> unconnected-(J9-Pad41)
- J9 pad 42: (no net) -> unconnected-(J9-Pad42)
- J9 pad 43: (no net) -> unconnected-(J9-Pad43)
- J9 pad 44: (no net) -> unconnected-(J9-Pad44)
- J9 pad 45: (no net) -> unconnected-(J9-Pad45)
- J9 pad 46: (no net) -> unconnected-(J9-Pad46)
- J9 pad 47: (no net) -> unconnected-(J9-Pad47)
- J9 pad 48: (no net) -> unconnected-(J9-Pad48)
- J9 pad 49: (no net) -> unconnected-(J9-Pad49)
- J9 pad 50: (no net) -> unconnected-(J9-Pad50)
- J9 pad 51: (no net) -> unconnected-(J9-Pad51)
- J9 pad 52: (no net) -> unconnected-(J9-Pad52)
- J9 pad 53: (no net) -> unconnected-(J9-Pad53)
- J9 pad 54: (no net) -> unconnected-(J9-Pad54)
- J9 pad 55: (no net) -> unconnected-(J9-Pad55)
- J9 pad 56: (no net) -> unconnected-(J9-Pad56)
- J9 pad 57: (no net) -> unconnected-(J9-Pad57)
- J9 pad 58: (no net) -> unconnected-(J9-Pad58)
- J9 pad 59: (no net) -> unconnected-(J9-Pad59)
- J9 pad 60: (no net) -> unconnected-(J9-Pad60)
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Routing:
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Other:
- copper layers 2 -> 4

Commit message: Correct Nets and Footprints
Updated the footprints with the correct nets. Some route may need to be redone but overall should be able to continue with layout without issue
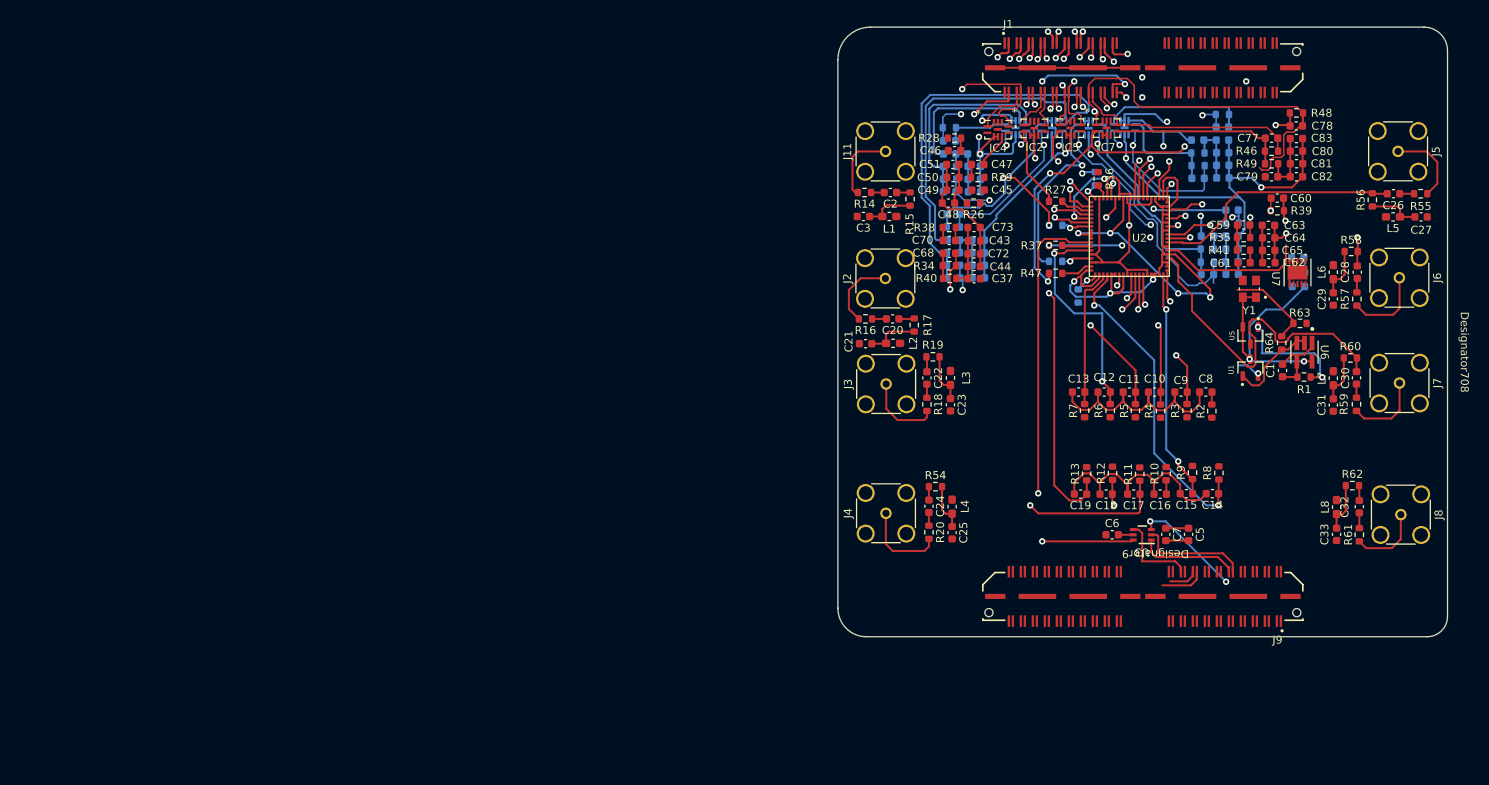
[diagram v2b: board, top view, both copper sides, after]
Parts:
- removed the C1 at (208.4, 71.8)
- removed the C10 at (192.4, 74.5)
- removed the C11 at (189.2, 74.5)
- removed the C12 at (186.1, 74.5)
- removed the C13 at (182.9, 74.5)
- removed the C14 at (199.6, 87.2)
- removed the C15 at (196.4, 87.2)
- removed the C16 at (193.1, 87.2)
- removed the C17 at (189.8, 87.2)
- removed the C18 at (186.3, 87.2)
- removed the C19 at (183.1, 87.2)
- removed the C2 at (159.4, 49.5)
- removed the C20 at (159.6, 65.3)
- removed the C21 at (156.3, 68.4)
- removed the C22 at (163.9, 72.7)
- removed the C23 at (166.9, 76.0)
- removed the C24 at (164.2, 88.7)
- removed the C25 at (167.1, 92.0)
- removed the C26 at (222.2, 49.7)
- removed the C27 at (225.7, 52.6)
- removed the C28 at (217.7, 59.5)
- removed the C29 at (214.7, 62.8)
- removed the C3 at (156.0, 52.5)
- removed the C30 at (217.6, 72.7)
- removed the C31 at (214.7, 76.1)
- removed the C32 at (218.0, 88.8)
- removed the C33 at (215.1, 92.2)
- removed the C34 at (210.3, 57.7)
- removed the C35 at (166.8, 49.4)
- removed the C36 at (166.7, 43.0)
- removed the C37 at (169.8, 60.3)
- removed the C38 at (166.8, 44.7)
- removed the C39 at (169.8, 46.2)
- removed the C4 at (210.4, 59.5)
- removed the C40 at (169.8, 47.9)
- removed the C41 at (169.9, 49.4)
- removed the C42 at (169.8, 44.7)
- removed the C43 at (169.9, 55.6)
- removed the C44 at (169.8, 58.8)
- removed the C45 at (170.3, 49.2)
- removed the C46 at (167.4, 44.3)
- removed the C47 at (170.3, 46.0)
- removed the C48 at (166.6, 50.8)
- removed the C49 at (167.2, 49.2)
- removed the C5 at (196.6, 92.2)
- removed the C50 at (167.2, 47.6)
- removed the C51 at (167.2, 46.0)
- removed the C52 at (167.3, 60.2)
- removed the C53 at (167.2, 52.2)
- removed the C54 at (167.3, 55.5)
- removed the C55 at (170.3, 55.5)
- removed the C56 at (170.3, 57.1)
- removed the C57 at (170.4, 58.6)
- removed the C58 at (170.4, 60.2)
- removed the C59 at (203.5, 53.6)
- removed the C6 at (187.1, 92.3)
- removed the C60 at (207.7, 50.2)
- removed the C61 at (203.6, 58.3)
- removed the C62 at (206.7, 58.3)
- removed the C63 at (206.6, 53.6)
- removed the C64 at (206.6, 55.2)
- removed the C65 at (206.6, 56.8)
- removed the C66 at (199.0, 59.8)
- removed the C67 at (202.1, 51.7)
- removed the C68 at (166.7, 57.1)
- removed the C69 at (199.0, 55.0)
- removed the C7 at (193.8, 92.2)
- removed the C70 at (166.7, 55.5)
- removed the C71 at (202.1, 59.7)
- removed the C72 at (169.8, 57.2)
- removed the C73 at (169.8, 53.9)
- removed the C74 at (202.1, 55.0)
- removed the C75 at (202.1, 58.2)
- removed the C76 at (202.1, 56.6)
- removed the C77 at (207.0, 42.7)
- removed the C78 at (210.1, 41.2)
- removed the C79 at (207.0, 47.5)
- removed the C8 at (198.8, 74.5)
- removed the C80 at (210.1, 44.3)
- removed the C81 at (210.1, 45.9)
- removed the C82 at (210.1, 47.5)
- removed the C83 at (210.1, 42.8)
- removed the C84 at (197.8, 47.7)
- removed the C85 at (200.9, 41.3)
- removed the C86 at (197.8, 43.0)
- removed the C87 at (200.9, 46.1)
- removed the C88 at (200.9, 44.5)
- removed the C89 at (200.9, 43.0)
- removed the C9 at (195.7, 74.5)
- removed the C90 at (200.9, 47.7)
- removed the IC1 at (175.0, 41.4)
- removed the IC2 at (177.3, 41.5)
- removed the IC3 at (179.5, 41.4)
- removed the IC4 at (172.8, 41.7)
- removed the IC5 at (181.9, 41.5)
- removed the IC6 at (184.2, 41.4)
- removed the IC7 at (186.4, 41.5)
- removed the IC8 at (188.6, 41.4)
- removed the J1 at (190.9, 33.9)
- removed the J11 at (158.7, 44.4)
- removed the J2 at (158.8, 60.2)
- removed the J3 at (158.8, 73.4)
- removed the J4 at (158.8, 89.6)
- removed the J5 at (223.0, 44.4)
- removed the J6 at (223.0, 60.2)
- removed the J7 at (223.0, 73.3)
- removed the J8 at (223.2, 89.8)
- removed the L1 at (159.2, 52.5)
- removed the L2 at (159.7, 68.4)
- removed the L3 at (166.9, 72.7)
- removed the L4 at (167.1, 88.8)
- removed the L5 at (222.2, 52.6)
- removed the L6 at (214.7, 59.5)
- removed the L7 at (214.7, 72.7)
- removed the L8 at (215.1, 88.8)
- removed the R1 at (211.1, 72.6)
- removed the R10 at (193.8, 84.7)
- removed the R11 at (190.5, 84.7)
- removed the R12 at (187.1, 84.6)
- removed the R13 at (183.9, 84.7)
- removed the R14 at (156.1, 49.5)
- removed the R15 at (161.8, 50.3)
- removed the R16 at (156.2, 65.3)
- removed the R17 at (162.3, 66.1)
- removed the R18 at (163.9, 76.0)
- removed the R19 at (164.7, 70.1)
- removed the R2 at (199.5, 76.8)
- removed the R20 at (164.2, 92.0)
- removed the R21 at (166.8, 47.8)
- removed the R22 at (185.0, 47.8)
- removed the R23 at (166.7, 41.4)
- removed the R24 at (166.7, 46.3)
- removed the R25 at (210.4, 61.3)
- removed the R26 at (169.8, 50.8)
- removed the R27 at (180.0, 50.6)
- removed the R28 at (167.4, 42.7)
- removed the R29 at (170.3, 47.6)
- removed the R3 at (196.4, 76.8)
- removed the R30 at (167.3, 58.6)
- removed the R31 at (180.0, 53.6)
- removed the R32 at (167.2, 53.8)
- removed the R33 at (167.3, 57.0)
- removed the R34 at (166.7, 58.7)
- removed the R35 at (203.5, 55.1)
- removed the R36 at (185.3, 47.8)
- removed the R37 at (180.0, 56.1)
- removed the R38 at (166.7, 53.9)
- removed the R39 at (207.7, 51.8)
- removed the R4 at (193.1, 76.8)
- removed the R40 at (166.8, 60.3)
- removed the R41 at (203.5, 56.7)
- removed the R42 at (199.0, 58.2)
- removed the R43 at (180.0, 58.1)
- removed the R44 at (202.1, 53.3)
- removed the R45 at (199.0, 56.6)
- removed the R46 at (207.0, 44.3)
- removed the R47 at (180.0, 59.6)
- removed the R48 at (210.1, 39.6)
- removed the R49 at (207.0, 45.9)
- removed the R5 at (190.0, 76.8)
- removed the R50 at (197.8, 46.2)
- removed the R51 at (182.8, 62.4)
- removed the R52 at (200.9, 39.8)
- removed the R53 at (197.8, 44.6)
- removed the R54 at (165.0, 86.3)
- removed the R55 at (225.6, 49.7)
- removed the R56 at (219.6, 50.4)
- removed the R57 at (217.7, 62.8)
- removed the R58 at (217.0, 56.9)
- removed the R59 at (217.6, 76.0)
- removed the R6 at (186.8, 76.8)
- removed the R60 at (216.9, 70.2)
- removed the R61 at (218.0, 92.3)
- removed the R62 at (217.1, 86.2)
- removed the R63 at (210.6, 65.9)
- removed the R64 at (208.3, 68.3)
- removed the R7 at (183.6, 76.8)
- removed the R8 at (200.4, 84.6)
- removed the R9 at (197.1, 84.5)
- removed the U1 at (204.4, 71.4)
- removed the U2 at (194.2, 50.0)
- removed the U3 at (190.8, 92.3)
- removed the U5 at (204.4, 67.4)
- removed the U6 at (211.1, 69.3)
- removed the U7 at (210.3, 59.5)
- removed the Y1 at (204.2, 61.6)
- C34, C35, C36, C38, C39, C4, C40, C41, C42, C52, C53, C54, C55, C56, C57, C58, C66, C67, C69, C71, C74, C75, C76, C84, C85, C86, C87, C88, C89, C90, IC1, IC3, IC6, IC8, R21, R22, R23, R24, R25, R30, R31, R32, R33, R42, R43, R44, R45, R50, R51, R52, R53: moved to B.Cu
- moved C26 171.5 mm to (222.2, 49.7)
- moved C27 169.9 mm to (225.7, 52.6)
- moved R55 166.4 mm to (225.6, 49.7)
- moved C32 164.5 mm to (218.0, 88.8), turned to -90 degrees
- moved C30 162.6 mm to (217.6, 72.7), turned to -90 degrees
- moved C28 162.1 mm to (217.7, 59.5), turned to -90 degrees
- moved C33 161.8 mm to (215.1, 92.2), turned to -90 degrees
- moved R56 160.6 mm to (219.6, 50.4), turned to 90 degrees
- moved C31 159.8 mm to (214.7, 76.1), turned to -90 degrees
- moved C29 159.2 mm to (214.7, 62.8), turned to -90 degrees
- moved J5 159.0 mm to (222.8, 44.4), turned to -90 degrees
- moved R61 158.3 mm to (218.0, 92.3), turned to -90 degrees
- moved R57 158.0 mm to (217.7, 62.8), turned to -90 degrees
- moved R59 155.7 mm to (217.6, 76.0), turned to -90 degrees
- moved R62 155.7 mm to (217.1, 86.2)
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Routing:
- net (no net): track 266.8 -> 0.00 mm, vias 12 -> 0
- net VDD33: track 0.00 -> 168.1 mm, vias 0 -> 10
- net V_OCM: track 0.00 -> 98.7 mm, vias 0 -> 2
